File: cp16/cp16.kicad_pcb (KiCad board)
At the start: 2 copper layers, 76.2 x 100 mm, 33 parts, among them J1 Conn_01x04, J2 Conn_01x04, J3 Conn_01x04, SW1 SW_Push, SW10 SW_Push, SW11 SW_Push, SW12 SW_Push, SW13 SW_Push, SW14 SW_Push, SW15 SW_Push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

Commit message: Routing
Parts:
- R1: value 4.7k -> SDA
- R2: value 4.7k -> SCL
- R3: value 100k -> ADDR1
- R4: value 100k -> ADDR2
- R5: value 100k -> ADDR4
- U2: footprint Package_DIP:DIP-28_W7.62mm_Socket -> Package_DIP:DIP-28_W7.62mm
- moved R2 10.0 mm to (90.2, 45.5), turned to -135 degrees
- moved R1 10.00 mm to (85.4, 45.5), turned to -135 degrees
- moved U1 0.89 mm to (64.0, 64.7)
- moved R3 0.10 mm to (87.8, 52.7)
- moved R4 0.07 mm to (92.6, 52.7)
- moved R5 0.06 mm to (97.4, 52.7)
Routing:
- net GND: track 0.00 -> 475.0 mm, vias 0 -> 3
- net +3V3: track 0.00 -> 140.3 mm, vias 0 -> 1
- net SW4: track 0.00 -> 119.6 mm, vias 0 -> 1
- net SW3: track 0.00 -> 105.5 mm, vias 0 -> 3
- net SCL: track 0.00 -> 95.7 mm, vias 0 -> 1
- net SW8: track 0.00 -> 93.1 mm, vias 0 -> 3
- net SDA: track 0.00 -> 88.1 mm, vias 0 -> 1
- net SW1: track 0.00 -> 87.5 mm, vias 0 -> 3
- net SW2: track 0.00 -> 86.1 mm, vias 0 -> 3
- net SW16: track 0.00 -> 81.9 mm, vias 0 -> 2
- net SW7: track 0.00 -> 75.8 mm, vias 0 -> 5
- net SW12: track 0.00 -> 74.6 mm, vias 0 -> 2
- net SW15: track 0.00 -> 63.5 mm, vias 0 -> 2
- net SW5: track 0.00 -> 62.1 mm, vias 0 -> 5
- net SW6: track 0.00 -> 59.5 mm, vias 0 -> 5
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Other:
- board text added: "cp16 v0.1 by 1.038"

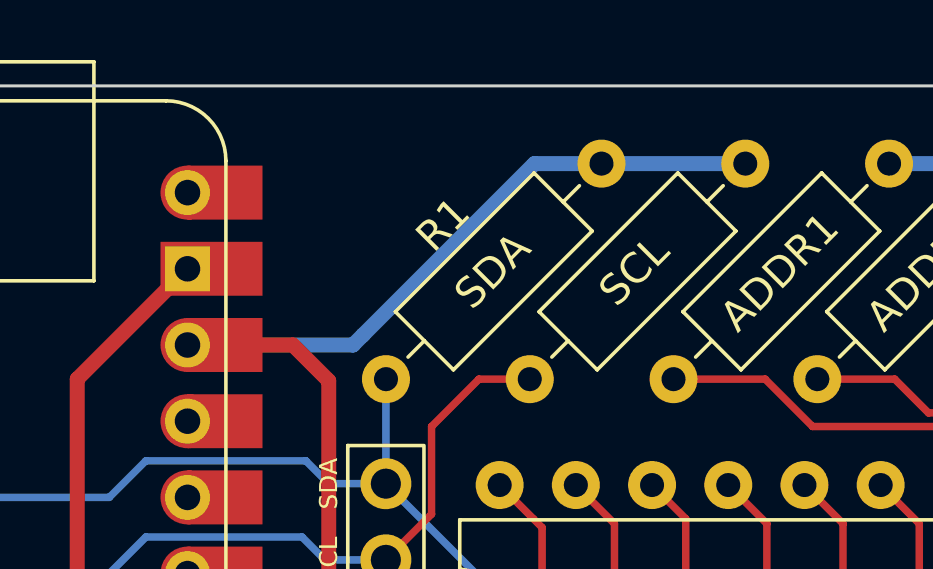
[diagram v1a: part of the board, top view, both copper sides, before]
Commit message: add logo
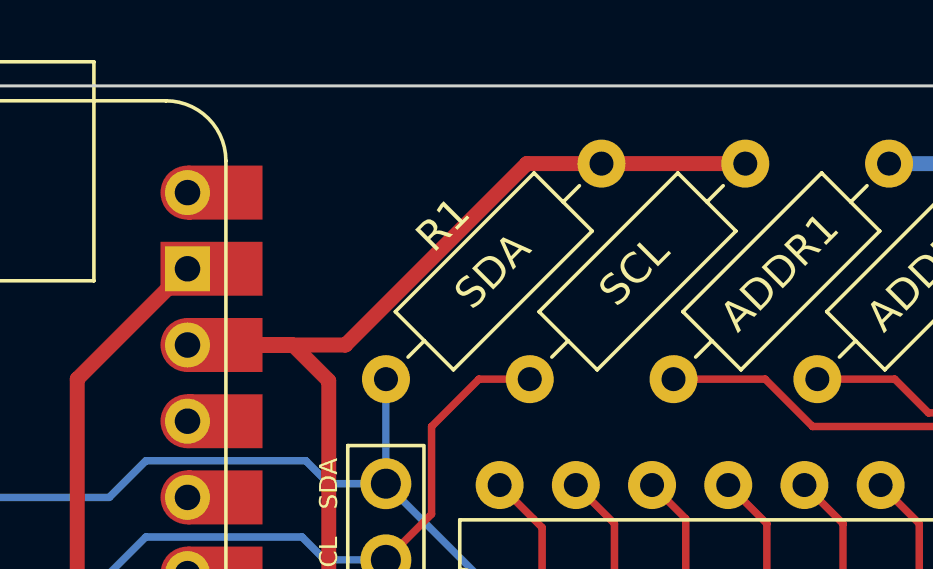
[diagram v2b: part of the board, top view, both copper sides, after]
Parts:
- added G***: LOGO, LOGO, B.Cu at (64.0, 52.7)
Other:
- board text added: "by 1.038 v0.1"
- board text removed: "cp16 v0.1 by 1.038"
